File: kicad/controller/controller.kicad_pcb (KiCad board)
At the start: 2 copper layers, 22.2 x 58.4 mm, 14 parts, among them J1 Screw_Terminal_01x08, J2 Raspberry_Pi_2_3

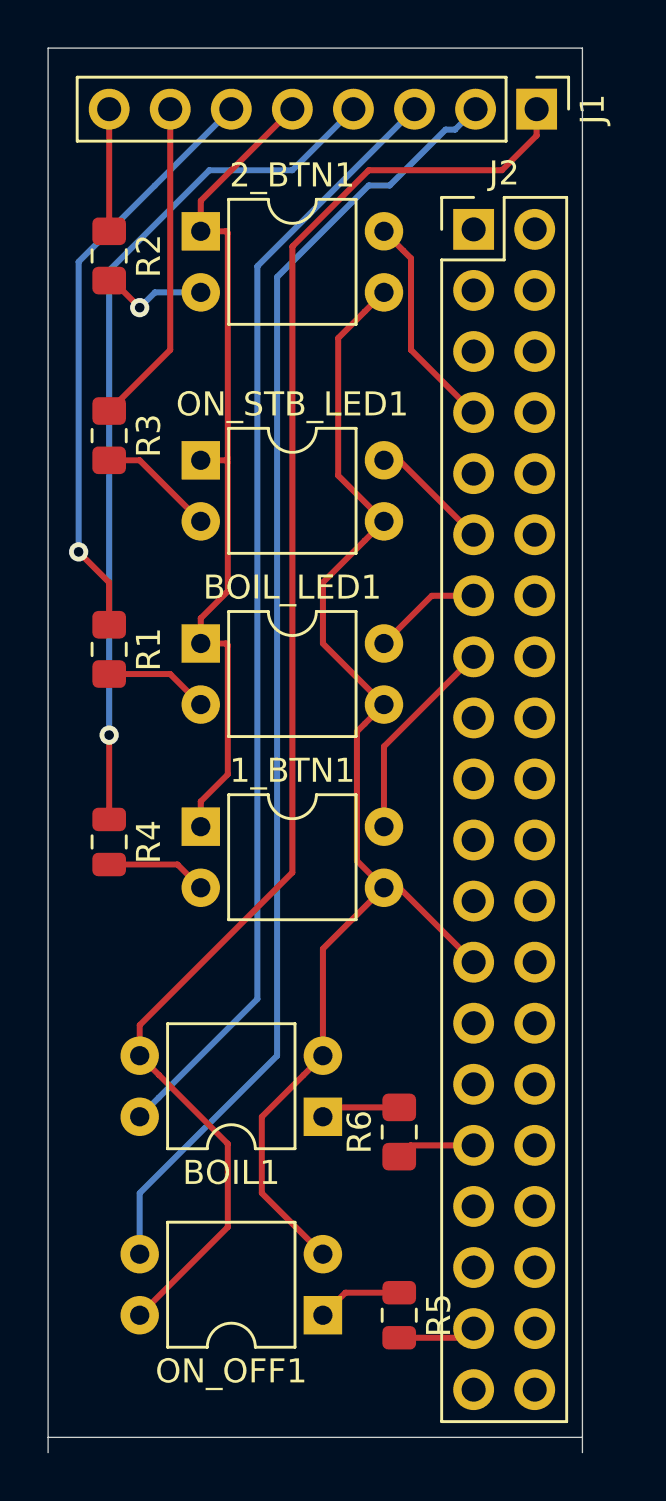
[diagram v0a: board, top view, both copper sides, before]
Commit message: Removing button readers
Not much point in reading the button 2 and needed button 2 wire for a wire I missed the first time
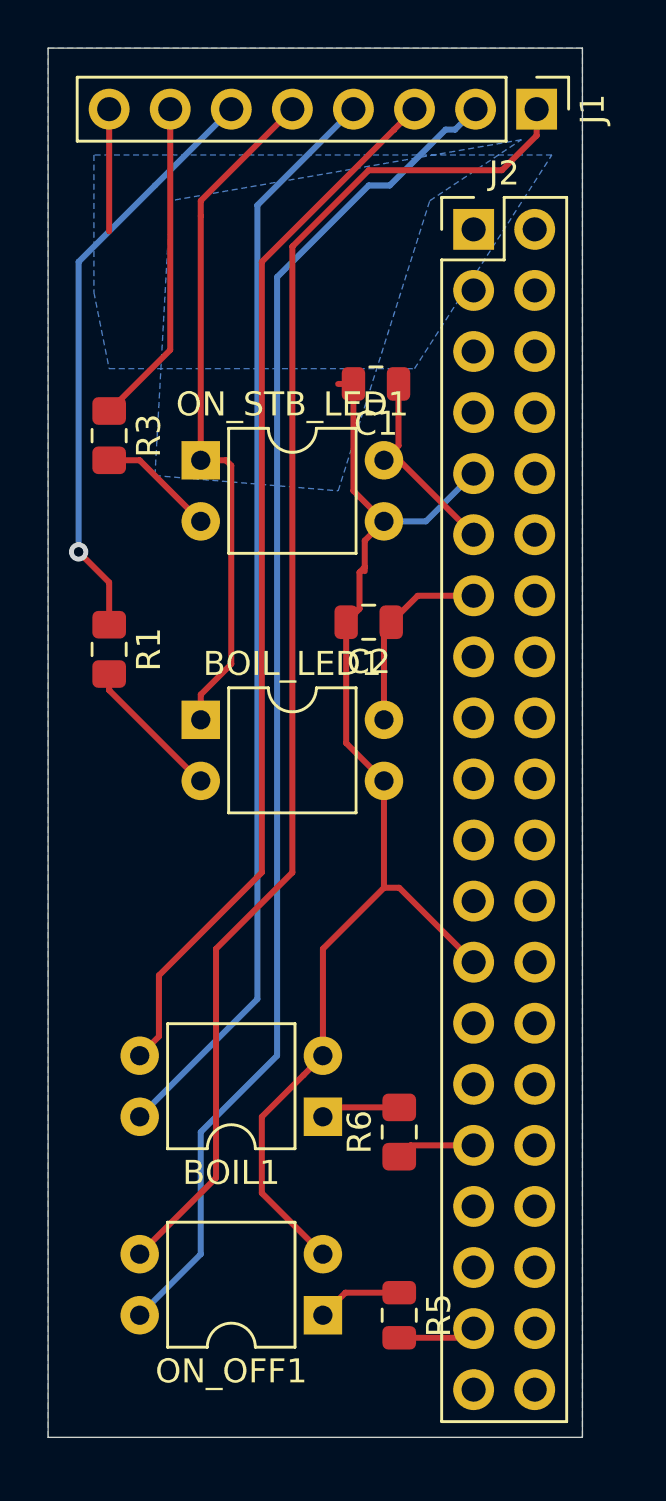
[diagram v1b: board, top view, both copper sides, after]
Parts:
- removed 1_BTN1, 2_BTN1: PC817, Package_DIP:DIP-4_W7.62mm
- removed R2: R_US, Resistor_SMD:R_0805_2012Metric_Pad1.15x1.40mm_HandSolder
- removed R4: R_US, Resistor_SMD:R_0805_2012Metric
- added C1: C, Capacitor_SMD:C_0805_2012Metric, F.Cu at (138.7, 66.7)
- added C2: C, Capacitor_SMD:C_0805_2012Metric, F.Cu at (138.4, 76.6)
- moved BOIL_LED1 3.17 mm to (131.4, 80.6)
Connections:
- J1 pad 1: Net-(BOIL1-Pad3) -> Net-(J1-Pad1)
- J1 pad 3: Net-(BOIL1-Pad4) -> Net-(BOIL1-Pad3)
- J1 pad 4: Net-(J1-Pad4) -> Net-(BOIL1-Pad4)
- J2 pad 9: Net-(J2-Pad9) -> GND
- ON_OFF1 pad 3: Net-(J1-Pad2) -> Net-(J1-Pad1)
- ON_OFF1 pad 4: Net-(BOIL1-Pad3) -> Net-(J1-Pad2)
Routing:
- net Net-(J1-Pad1): track 0.00 -> 57.7 mm
- net Net-(J1-Pad4): track 35.8 -> 0.00 mm, vias 1 -> 0
- net Net-(BOIL1-Pad3): track 63.3 -> 44.1 mm
- net Net-(J2-Pad7): track 9.09 -> 0.00 mm
- net Net-(J2-Pad15): track 8.61 -> 0.00 mm
- net Net-(BOIL_LED1-Pad1): track 35.6 -> 28.6 mm
- net Net-(2_BTN1-Pad2): track 4.54 -> 0.00 mm, vias 1 -> 0
- net Net-(1_BTN1-Pad2): track 4.21 -> 0.00 mm
- net Net-(BOIL_LED1-Pad4): track 4.55 -> 8.07 mm
- net Net-(C1-Pad1): track 5.01 -> 8.44 mm
- net Net-(J1-Pad2): track 54.2 -> 56.7 mm
- net Net-(BOIL_LED1-Pad2): track 4.34 -> 6.05 mm
- net GND: track 52.8 -> 51.5 mm
- net Net-(BOIL1-Pad4): track 46.6 -> 45.6 mm
- added copper zone on B.Cu, net GND
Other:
- board size 22.2 x 58.4 mm -> 22.2 x 57.8 mm
- board text added: "https://github.com/fiveohhh/s1-controller v2"

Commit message: Updating pcb file
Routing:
- net Net-(J1-Pad8): track 5.08 -> 0.00 mm
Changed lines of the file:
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@@
     (thickness 1.6)
     (drawings 5)
-    (tracks 88)
+    (tracks 87)
     (zones 0)
     (modules 12)
@@
   (layers
     (0 F.Cu signal)
-    (31 B.Cu signal hide)
+    (31 B.Cu signal)
     (32 B.Adhes user)
     (33 F.Adhes user)
@@
   (segment (start 126.365 61.595) (end 129.54 58.42) (width 0.25) (layer B.Cu) (net 1))
   (segment (start 126.365 73.66) (end 126.365 61.595) (width 0.25) (layer B.Cu) (net 1))
-  (segment (start 127.635 60.325) (end 127.635 55.245) (width 0.25) (layer F.Cu) (net 2))
   (segment (start 130.175 65.26) (end 130.175 55.245) (width 0.25) (layer F.Cu) (net 3))
   (segment (start 127.635 67.8) (end 130.175 65.26) (width 0.25) (layer F.Cu) (net 3))
@@
   (segment (start 131.445 97.79) (end 131.445 102.87) (width 0.25) (layer B.Cu) (net 7))
   (segment (start 134.62 94.615) (end 131.445 97.79) (width 0.25) (layer B.Cu) (net 7))
-  (segment (start 139.7 69.85) (end 139.065 69.85) (width 0.25) (layer F.Cu) (net 47))
-  (segment (start 142.795001 72.945001) (end 139.7 69.85) (width 0.25) (layer F.Cu) (net 47))
   (segment (start 140.169999 98.345001) (end 139.7 98.815) (width 0.25) (layer F.Cu) (net 32))
   (segment (start 142.795001 98.345001) (end 140.169999 98.345001) (width 0.25) (layer F.Cu) (net 32))
   (segment (start 142.412502 106.3475) (end 142.795001 105.965001) (width 0.25) (layer F.Cu) (net 37))
   (segment (start 139.7 106.3475) (end 142.412502 106.3475) (width 0.25) (layer F.Cu) (net 37))
-  (segment (start 131.445 59.055) (end 135.255 55.245) (width 0.25) (layer F.Cu) (net 50))
   (segment (start 133.80001 59.23999) (end 137.795 55.245) (width 0.25) (layer B.Cu) (net 40))
   (segment (start 128.905 97.155) (end 133.80001 92.25999) (width 0.25) (layer B.Cu) (net 40))
@@
   (segment (start 133.985 61.59359) (end 139.483591 56.094999) (width 0.25) (layer F.Cu) (net 41))
   (segment (start 133.985 86.995) (end 133.985 61.59359) (width 0.25) (layer F.Cu) (net 41))
-  (segment (start 135.255 60.96) (end 138.43 57.785) (width 0.25) (layer F.Cu) (net 48))
-  (segment (start 135.255 86.995) (end 135.255 60.96) (width 0.25) (layer F.Cu) (net 48))
-  (segment (start 145.415 56.345) (end 145.415 55.245) (width 0.25) (layer F.Cu) (net 48))
-  (segment (start 143.975 57.785) (end 145.415 56.345) (width 0.25) (layer F.Cu) (net 48))
-  (segment (start 138.43 57.785) (end 143.975 57.785) (width 0.25) (layer F.Cu) (net 48))
   (segment (start 136.915 96.765) (end 136.525 97.155) (width 0.25) (layer F.Cu) (net 42))
   (segment (start 139.7 96.765) (end 136.915 96.765) (width 0.25) (layer F.Cu) (net 42))
@@
   (segment (start 128.905 69.85) (end 131.445 72.39) (width 0.25) (layer F.Cu) (net 46))
   (segment (start 127.635 69.85) (end 128.905 69.85) (width 0.25) (layer F.Cu) (net 46))
+  (segment (start 139.7 69.85) (end 139.065 69.85) (width 0.25) (layer F.Cu) (net 47))
+  (segment (start 142.795001 72.945001) (end 139.7 69.85) (width 0.25) (layer F.Cu) (net 47))
+  (segment (start 139.67 69.245) (end 139.065 69.85) (width 0.25) (layer F.Cu) (net 47))
+  (segment (start 139.67 66.675) (end 139.67 69.245) (width 0.25) (layer F.Cu) (net 47))
+  (segment (start 135.255 60.96) (end 138.43 57.785) (width 0.25) (layer F.Cu) (net 48))
+  (segment (start 135.255 86.995) (end 135.255 60.96) (width 0.25) (layer F.Cu) (net 48))
+  (segment (start 145.415 56.345) (end 145.415 55.245) (width 0.25) (layer F.Cu) (net 48))
+  (segment (start 143.975 57.785) (end 145.415 56.345) (width 0.25) (layer F.Cu) (net 48))
+  (segment (start 138.43 57.785) (end 143.975 57.785) (width 0.25) (layer F.Cu) (net 48))
+  (segment (start 128.905 102.87) (end 132.08 99.695) (width 0.25) (layer F.Cu) (net 48))
+  (segment (start 132.08 99.695) (end 132.08 90.17) (width 0.25) (layer F.Cu) (net 48))
+  (segment (start 132.08 90.17) (end 135.255 86.995) (width 0.25) (layer F.Cu) (net 48))
+  (segment (start 131.445 59.055) (end 135.255 55.245) (width 0.25) (layer F.Cu) (net 50))
   (segment (start 131.445 79.595) (end 132.715 78.325) (width 0.25) (layer F.Cu) (net 50))
   (segment (start 131.445 80.645) (end 131.445 79.595) (width 0.25) (layer F.Cu) (net 50))
@@
   (segment (start 132.715 70.07) (end 132.495 69.85) (width 0.25) (layer F.Cu) (net 50))
   (segment (start 132.715 78.325) (end 132.715 70.07) (width 0.25) (layer F.Cu) (net 50))
-  (segment (start 139.67 69.245) (end 139.065 69.85) (width 0.25) (layer F.Cu) (net 47))
-  (segment (start 139.67 66.675) (end 139.67 69.245) (width 0.25) (layer F.Cu) (net 47))
-  (segment (start 128.905 102.87) (end 132.08 99.695) (width 0.25) (layer F.Cu) (net 48))
-  (segment (start 132.08 99.695) (end 132.08 90.17) (width 0.25) (layer F.Cu) (net 48))
-  (segment (start 132.08 90.17) (end 135.255 86.995) (width 0.25) (layer F.Cu) (net 48))
   (segment (start 131.445 69.85) (end 131.445 59.69) (width 0.25) (layer F.Cu) (net 50))
   (segment (start 131.445 59.69) (end 131.445 59.055) (width 0.25) (layer F.Cu) (net 50))
